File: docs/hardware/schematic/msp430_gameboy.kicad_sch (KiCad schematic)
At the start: 27 parts, among them J1 OLED_SPI, J2 LiPo_Charger, SW1 SW_BTN_A, SW2 SW_BTN_B, SW3 SW_BTN_C, SW4 SW_BTN_D, SW5 SW_BTN_E, SW6 SW_BTN_F, SW7 SW_BTN_G, SW8 SW_BTN_H, U1 MSP430G2553, U2 SN74HC165N, U3 LM386N-1

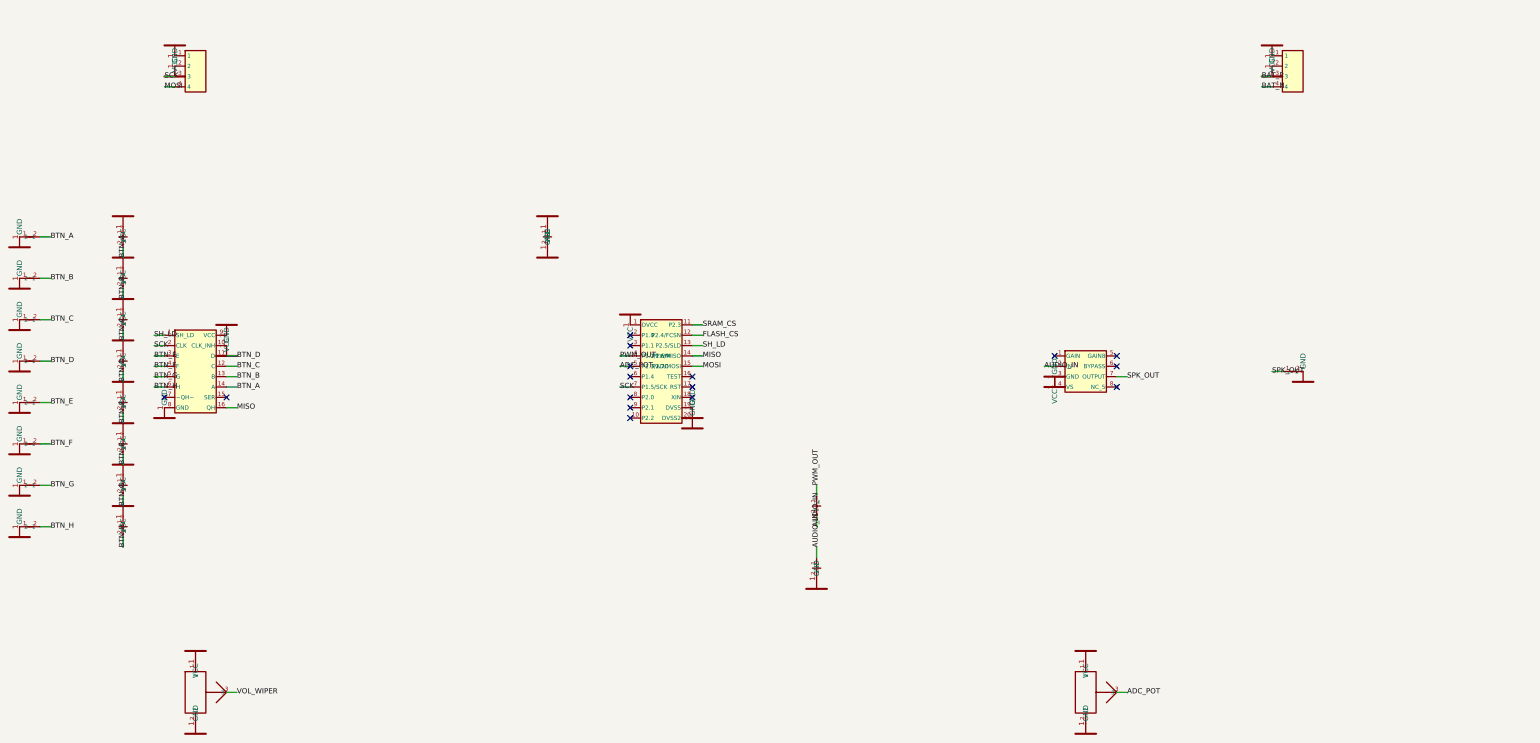
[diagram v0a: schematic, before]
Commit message: refactor: rewrite gen_kicad7.py to use KiCad built-in libraries; center MSP430 in schematic
- gen_kicad7.py now parses KiCad's installed .kicad_sym libraries at runtime
  and embeds real symbols (with proper 'extends' handling) for:
  MSP430G2553IN20, 74HC165, LM386, W25Q128JVS, Device:R, Device:C
- Custom symbols generated for: 23LC1024 SRAM, OLED 7-pin connector,
  LiPo 4-pin connector, Speaker, SW_Push, VCC/GND power
- Layout redesigned: MSP430 at center, peripherals radiate outward
  (OLED/SRAM/Flash above; SR+buttons left; LM386+speaker right)
- Fixes: SH_LD on P2.5 (not P2.4), FLASH_CS on P2.4, all CS labels correct
- Adds SRAM (23LC1024) and Flash (W25Q128JVS) as placed symbols
- Removes ADC pot (RV2) — not in BOM
- Expands OLED connector from 4 to 7 pins (GND/VCC/SCLK/MOSI/RST/DC/CS)
- Output path fixed to docs/hardware/schematic/msp430_gameboy.kicad_sch
- Delete docs/hardware/notes/ (session notes extracted to memory)

Co-Authored-By: Claude Sonnet 4.6 <noreply@anthropic.com>
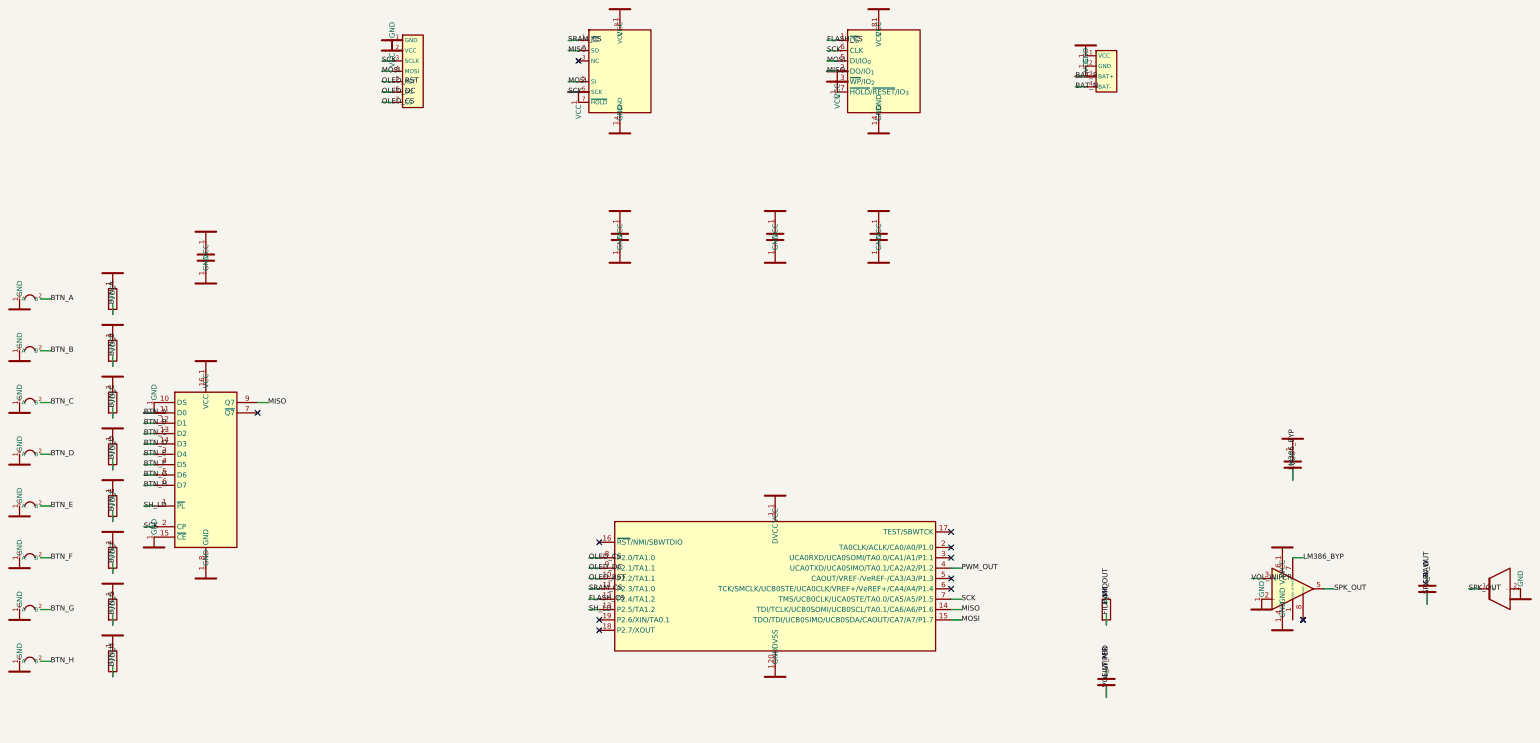
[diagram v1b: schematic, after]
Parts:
- removed C1, C2: 100nF, symbol C
- removed J1: OLED_SPI, symbol Conn_01x04
- removed J2: LiPo_Charger, symbol Conn_01x04
- removed R1: 1k, symbol R
- removed R2, R3, R4, R5, R6, R7, R8, R9: 10k, symbol R
- removed RV1, RV2: 10k, symbol POT
- removed U1: MSP430G2553, symbol MSP430G2553
- removed U2: SN74HC165N, symbol SN74HC165N
- removed U3: LM386N-1, symbol LM386N
- added C1, C2, C3, C4: 100nF, symbol Device:C
- added C5, C6: 10uF, symbol Device:C
- added C7: 220uF, symbol Device:C
- added J1: SSD1325_OLED, symbol Conn_OLED_7
- added J2: LiPo_Charger, symbol Conn_LiPo_4
- added R1: 1k, symbol Device:R
- added R2, R3, R4, R5, R6, R7, R8, R9: 10k, symbol Device:R
- added U1: MSP430G2553, symbol MCU_Texas_MSP430:MSP430G2553IN20
- added U2: SN74HC165N, symbol 74xx:74HC165
- added U3: LM386N-1, symbol Amplifier_Audio:LM386
- added U4: 23LC1024-I/P, symbol SRAM_23LC1024
- added U5: W25Q128JVSSIQ, symbol Memory_Flash:W25Q128JVS
- LS1: value SP-3605 8R -> SP-3605
- SW1: value SW_BTN_A -> BTN_A
- SW2: value SW_BTN_B -> BTN_B
- SW3: value SW_BTN_C -> BTN_C
- SW4: value SW_BTN_D -> BTN_D
- SW5: value SW_BTN_E -> BTN_E
- SW6: value SW_BTN_F -> BTN_F
- SW7: value SW_BTN_G -> BTN_G
- SW8: value SW_BTN_H -> BTN_H
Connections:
- net BAT_N: now also J2.4 (BAT-)
- net BAT_P: now also J2.3 (BAT+)
- net BTN_A: now also R2.2
- net BTN_B: now also R3.2
- net BTN_C: now also R4.2
- net BTN_D: now also R5.2
- net BTN_E: now also R6.2
- net BTN_F: now also R7.2
- net BTN_G: now also R8.2
- net BTN_H: now also R9.2
- net GND: now also C1.2, C2.2, C3.2, C4.2, J1.1 (GND), J2.2 (GND), U3.2 (-), U3.4 (GND), U4.4 (GND)
- net MISO: now also U4.2 (SO)
- net MOSI: now also J1.4 (MOSI), U4.5 (SI)
- net PWM_OUT: now also R1.1
- net SCK: now also J1.3 (SCLK), U4.6 (SCK)
- net SPK_OUT: now also C7.1, U3.5
- net SRAM_CS: now also U4.1 (~{CS})
- net VCC: now also C1.1, C2.1, C3.1, C4.1, C6.1, J1.2 (VCC), J2.1 (VCC), R2.1, R3.1, R4.1, R5.1, R6.1, R7.1, R8.1, R9.1, U3.6 (V+), U4.7 (~{HOLD}), U4.8 (VCC)
- net VOL_WIPER: now also C5.2, U3.3 (+)
- new net FILT_MID: C5.1, R1.2
- new net LM386_BYP: C6.2, U3.7 (BYPASS)
- new net OLED_CS: J1.7 (CS)
- new net OLED_DC: J1.6 (DC)
- new net OLED_RST: J1.5 (RST)
- new net SPK_RAW: C7.2
- no-connect marks 16 -> 12
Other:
- title: MSP430G2553 Game Boy -> MSP430G2553 Handheld Game Console
